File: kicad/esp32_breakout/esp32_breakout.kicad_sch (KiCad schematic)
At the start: 21 parts, among them J1 JST PH 2mm 7-pin male thru ve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, J2 JST PH 5-pin male thru vertic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, J3 JST PH 6-pin male thru vertic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, J4 Barrel_Jack, J5 JST PH 5-pin male thru vertic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, J6 JST PH 6-pin male thru vertic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, J7 JST PH 6-pin male thru vertic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, Q1 BSS123, SW1 SS12D10, U1 ESP32 DEV KIT DOIT 30-pin, U2 MH-KC24

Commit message: KiCad PCB schematic
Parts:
- added J10, J14: Conn_02x04_Top_Bottom, Connector_PinHeader_2.54mm:PinHeader_2x04_P2.54mm_Vertical, symbol Connector_Generic:Conn_02x04_Top_Bottom
- added J11, J12, J13: JST PH 6-pin male thru vertical, Connector_JST:JST_PH_B6B-PH-K_1x06_P2.00mm_Vertical, symbol Connector_Generic:Conn_01x06
- added J8: Conn_01x05, Connector_PinHeader_2.54mm:PinHeader_1x05_P2.54mm_Vertical, symbol Connector_Generic:Conn_01x05
- added J9: Conn_01x03, Connector_PinHeader_2.54mm:PinHeader_1x03_P2.54mm_Vertical, symbol Connector_Generic:Conn_01x03
- added R10: 10k, Resistor_SMD:R_0603_1608Metric, symbol Device:R_Small_US
- D1: value 1N4004 -> CGRA4004-G; footprint (none) -> Diode_SMD:D_SMA
- J4: value Barrel_Jack -> DC-005 5.5x2.1mm; footprint (none) -> Connector_BarrelJack:BarrelJack_GCT_DCJ200-10-A_Horizontal
- SW1: footprint (none) -> Library:SIP-3
- U1: footprint (none) -> Library:DIP-30_1000_ELL
- U2: value MH-KC24 -> Mini560-Pro; footprint (none) -> Library:SOIC-4; Link https://www.aliexpress.us/item/3256802247317350.html -> https://www.aliexpress.us/item/3256801443409123.html; Type USB Step Down Module 24V Dual Output -> DC-DC Module
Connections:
- net TOUCH6_TBD is gone; now on net I2C_INT: U1.26 (RTC_GPIO16/HSPI_CLK/TOUCH6/ADC2_CH6/GPIO14_BOOT_PWM)
- net +24V: now also U2.4 (VIN+); no longer U2.1 (VIN)
- net +3V3: now also J11.2 (Pin_2), J12.2 (Pin_2), J13.2 (Pin_2), J14.5 (Pin_5), J14.6 (Pin_6), J14.7 (Pin_7), J14.8 (Pin_8)
- net +5V: now also U2.3 (VOUT+), J11.1 (Pin_1), J12.1 (Pin_1), J13.1 (Pin_1), J14.1 (Pin_1), J14.2 (Pin_2), J14.3 (Pin_3), J14.4 (Pin_4), J8.1 (Pin_1), J9.1 (Pin_1); no longer U2.2 (VOUT)
- net GND: now also U2.1 (VIN-), U2.2 (VOUT-), J10.5 (Pin_5), J10.6 (Pin_6), J10.7 (Pin_7), J10.8 (Pin_8), J11.6 (Pin_6), J12.6 (Pin_6), J13.6 (Pin_6), J8.4 (Pin_4), J8.5 (Pin_5), J9.3 (Pin_3); no longer J5.3 (Pin_3), U1.23 (RTC_GPIO6/DAC1/ADC2_CH8/GPIO25), U2.3 (GND)
- net I2C_INT: now also J11.5 (Pin_5), J12.5 (Pin_5), J13.5 (Pin_5); no longer U1.18 (RTC_GPIO3/SENSOR_VN/ADC1_CH3/GPIO39_IN)
- net I2C_SCL: now also J11.3 (Pin_3), J12.3 (Pin_3), J13.3 (Pin_3)
- net I2C_SDA: now also J11.4 (Pin_4), J12.4 (Pin_4), J13.4 (Pin_4)
- net GPIO5_BOOT_STRAP: now reaches U1.8 (BOOT_PWM_GPIO5/VSPI_CS0)
- net GPIO5_BOOT_STRAP: now also J9.2 (Pin_2)
- net SERVO_LEFT renamed GPIO26_TOUCH
- net GPIO26_TOUCH: now also J10.3 (Pin_3)
- net SERVO_RIGHT renamed GPIO27_TOUCH
- net GPIO27_TOUCH: now also J10.2 (Pin_2)
- net TOUCH0 renamed GPIO4_TOUCH
- net GPIO4_TOUCH: now also J10.4 (Pin_4)
- net TOUCH5_TBD renamed GPIO12_OUT_STRAP
- net GPIO12_OUT_STRAP: now also J8.2 (Pin_2)
- net TOUCH9 renamed GPIO32_TOUCH
- net GPIO32_TOUCH: now also J10.1 (Pin_1)
- new net: J8.3 (Pin_3), R10.2
- new net GPIO39_IN: R10.1, U1.18 (RTC_GPIO3/SENSOR_VN/ADC1_CH3/GPIO39_IN)
- new net MOT_CW_RIGHT: J5.3 (Pin_3), U1.23 (RTC_GPIO6/DAC1/ADC2_CH8/GPIO25)
- no-connect marks 5 -> 4
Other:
- note added: "GPIO"
- note added: "I2C EXPANSION"
- note added: "LASER POINTER"
- note added: "SONAR"
- note removed: "BATTERY CONNECTOR"
- note removed: "EXPANSION"
- note removed: "TODO - on/off switch footprint - sonar conn? radar conn? - Try GPIO14_BOOT_PWM TOUCH6 - Try GPIO12_OUT TOUCH5 - regulator module connections - charger? - ESP32 footprint - TOUCH connector?"
- moved on the sheet: J3, J4, J6, J7, R5, R6, R9, SW1, U1

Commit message: Schematic WIP
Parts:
- removed J14: Conn_02x04_Top_Bottom, Connector_PinHeader_2.54mm:PinHeader_2x04_P2.54mm_Vertical, symbol Connector_Generic:Conn_02x04_Top_Bottom
- removed J4: DC-005 5.5x2.1mm, Connector_BarrelJack:BarrelJack_GCT_DCJ200-10-A_Horizontal, symbol Connector:Barrel_Jack
- removed SW1: SS12D10, Library:SIP-3, symbol Switch:SW_SPST
- added J4: DC-005 5.5x2.1mm, Connector_BarrelJack:BarrelJack_GCT_DCJ200-10-A_Horizontal, symbol Connector:Barrel_Jack_Switch
- added J5: Deans T-Plug M, Makerspet:DEANS-T-PLUG, symbol Makerspet:Deans T-Plug
- added SW1: SS12D10, Makerspet:SWITCH, symbol Switch:SW_SPDT
- J1: renamed from J5; value JST PH 5-pin male thru vertical -> JST PH F
- J10: renamed from J6; value JST PH 6-pin male thru vertical -> JST PH F
- J11: renamed from J7; value JST PH 6-pin male thru vertical -> JST PH F
- J12: renamed from J11; value JST PH 6-pin male thru vertical -> JST PH F
- J13: renamed from J12; value JST PH 6-pin male thru vertical -> JST PH F
- J14: renamed from J13; value JST PH 6-pin male thru vertical -> JST PH F
- J2: value JST PH 5-pin male thru vertical -> JST PH F
- J3: renamed from J1; value JST PH 2mm 7-pin male thru vertical -> JST PH F; footprint (none) -> Connector_JST:JST_PH_B7B-PH-K_1x07_P2.00mm_Vertical
- J6: renamed from J10; value Conn_02x04_Top_Bottom -> Header F
- J7: renamed from J8; value Conn_01x05 -> Header F
- J8: renamed from J9; value Conn_01x03 -> Header F
- J9: renamed from J3; value JST PH 6-pin male thru vertical -> JST PH F
- U1: value ESP32 DEV KIT DOIT 30-pin -> ESP32 DEV KIT 30-pin; footprint Library:DIP-30_1000_ELL -> Makerspet:ESP-32; symbol Kaia_v2:ESP32-DOIT-V1 -> Makerspet:ESP32-DOIT-V1
- U2: footprint Library:SOIC-4 -> Makerspet:Mini560-Pro; symbol Snoopy:USB-Step-Down-Converter -> Makerspet:DC-DC
- renumbered R2 to R1, R9 to R10, R4 to R2, R1 to R4, R8 to R5, R7 to R6, R10 to R7, R5 to R8, R6 to R9
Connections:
- net +24V: now also SW1.2 (B)
- net +3V3: now also J6.6 (Pin_6)
- net +5V: now also J6.5 (Pin_5)
- net GND: now also J4.2, J5.2 (BAT-); no longer J6.5 (Pin_5), J6.6 (Pin_6)
- new net +BATT: J4.1, J5.1 (BAT+), SW1.1 (A)
- no-connect marks 4 -> 6
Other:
- note added: "- add T plug - DC-005 as charger plug - BEFORE switch - IN CASE battery charges from input - barrel jack location?"
- company: REMAKE.AI -> Maker's Pet
- title: ESP32 Breakout -> Maker's Pet ESP32 Breakout
- moved on the sheet: J10, J11, J12, J13, J14, J6, J7, J8, R7

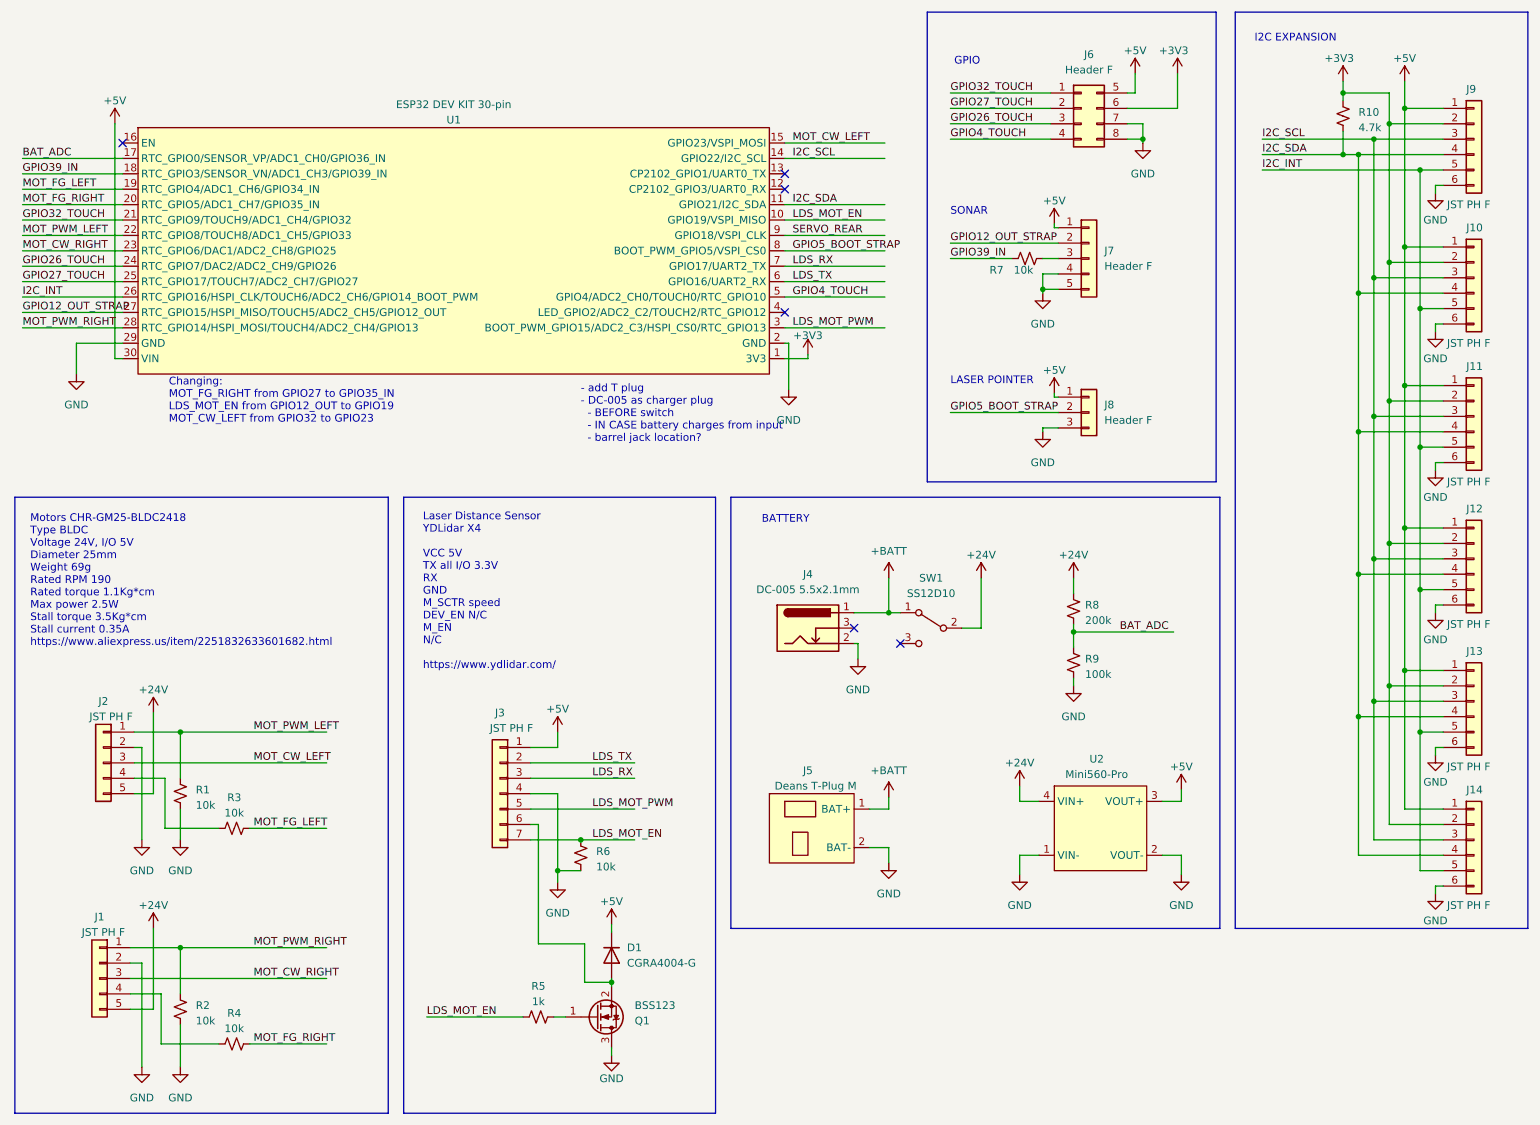
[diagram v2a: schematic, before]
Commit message: Fix broken fw; ESP32 schematic
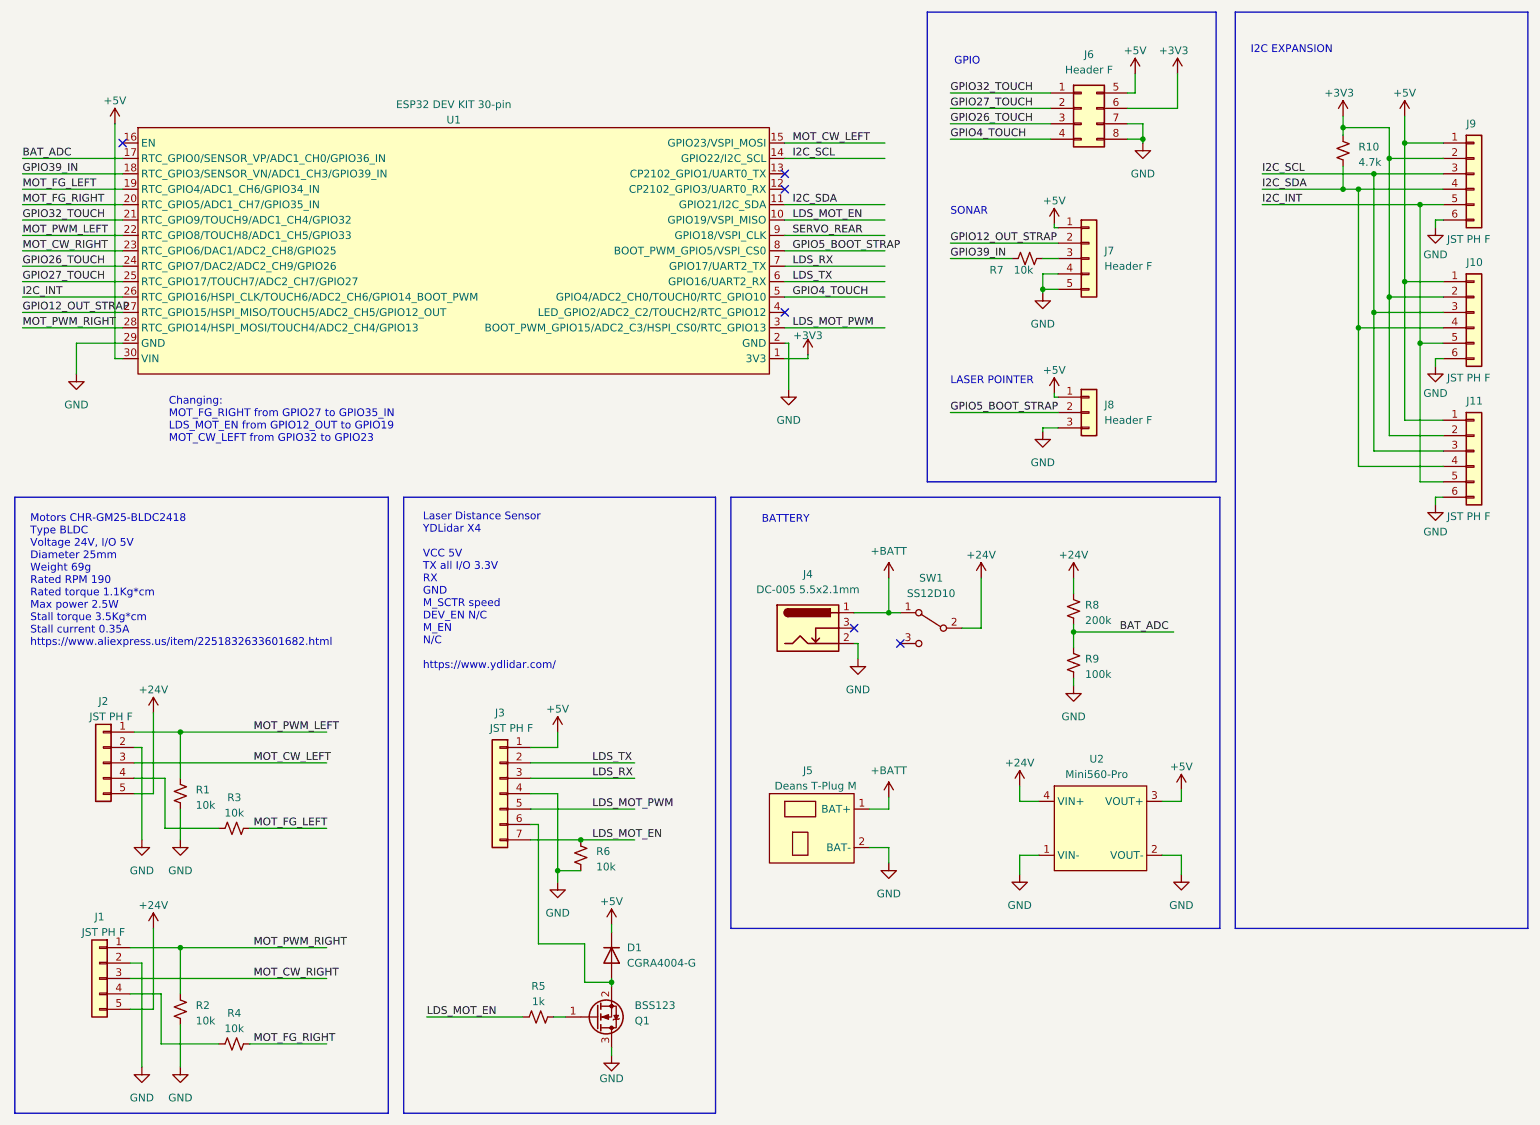
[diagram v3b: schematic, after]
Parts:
- removed J12, J13, J14: JST PH F, Connector_JST:JST_PH_B6B-PH-K_1x06_P2.00mm_Vertical, symbol Connector_Generic:Conn_01x06
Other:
- note removed: "- add T plug - DC-005 as charger plug - BEFORE switch - IN CASE battery charges from input - barrel jack location?"
- moved on the sheet: J10, J11, J9, R10

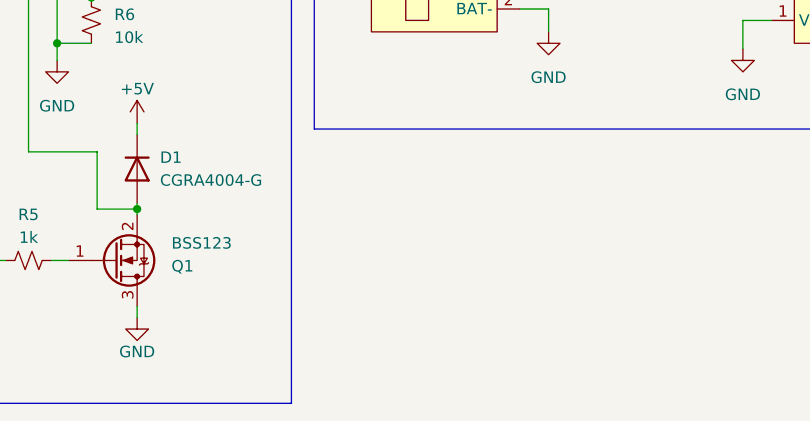
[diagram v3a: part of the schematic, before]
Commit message: Layout DRC pass
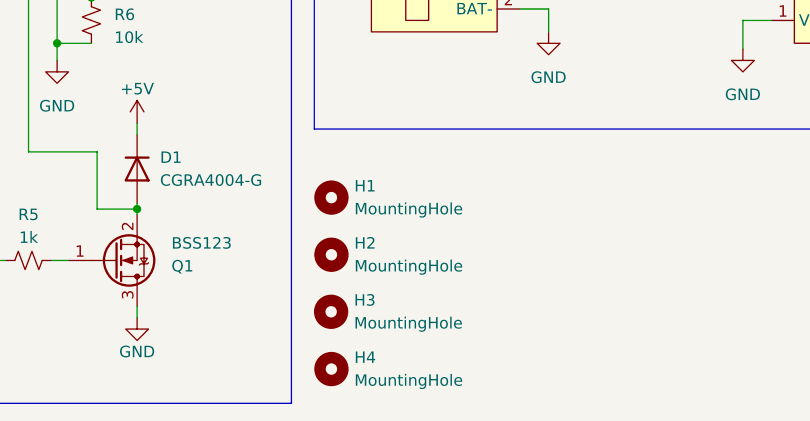
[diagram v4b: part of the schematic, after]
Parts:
- added H1, H2, H3, H4: MountingHole, MountingHole:MountingHole_3.2mm_M3, symbol Mechanical:MountingHole
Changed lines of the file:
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@@
+    )
+  )
+  (symbol (lib_id "Mechanical:MountingHole") (at 134.62 173.99 0) (unit 1)
+    (in_bom yes) (on_board yes) (dnp no) (fields_autoplaced)
+    (property "Reference" "H1" (at 137.16 172.72 0)
+      (effects (font (size 1.27 1.27)) (justify left))
+    )
+    (property "Value" "MountingHole" (at 137.16 175.26 0)
+      (effects (font (size 1.27 1.27)) (justify left))
+    )
+    (property "Footprint" "MountingHole:MountingHole_3.2mm_M3" (at 134.62 173.99 0)
+      (effects (font (size 1.27 1.27)) hide)
+    )
+    (property "Datasheet" "~" (at 134.62 173.99 0)
+      (effects (font (size 1.27 1.27)) hide)
+    )
+    (instances
+      (project "esp32_breakout"
+        (path "/e24ae185-8f18-408c-aee8-f727519bade3"
+          (reference "H1") (unit 1)
+        )
+      )
     )
   )
@@
         (path "/e24ae185-8f18-408c-aee8-f727519bade3"
           (reference "#PWR029") (unit 1)
+        )
+      )
+    )
+  )
+  (symbol (lib_id "Mechanical:MountingHole") (at 134.62 193.04 0) (unit 1)
+    (in_bom yes) (on_board yes) (dnp no) (fields_autoplaced)
+    (property "Reference" "H4" (at 137.16 191.77 0)
+      (effects (font (size 1.27 1.27)) (justify left))
+    )
+    (property "Value" "MountingHole" (at 137.16 194.31 0)
+      (effects (font (size 1.27 1.27)) (justify left))
+    )
+    (property "Footprint" "MountingHole:MountingHole_3.2mm_M3" (at 134.62 193.04 0)
+      (effects (font (size 1.27 1.27)) hide)
+    )
+    (property "Datasheet" "~" (at 134.62 193.04 0)
+      (effects (font (size 1.27 1.27)) hide)
+    )
+    (instances
+      (project "esp32_breakout"
+        (path "/e24ae185-8f18-408c-aee8-f727519bade3"
+          (reference "H4") (unit 1)
         )
       )
@@
     )
   )
+  (symbol (lib_id "Mechanical:MountingHole") (at 134.5851 186.6785 0) (unit 1)
+    (in_bom yes) (on_board yes) (dnp no) (fields_autoplaced)
+    (property "Reference" "H3" (at 137.1251 185.4085 0)
+      (effects (font (size 1.27 1.27)) (justify left))
+    )
+    (property "Value" "MountingHole" (at 137.1251 187.9485 0)
+      (effects (font (size 1.27 1.27)) (justify left))
+    )
+    (property "Footprint" "MountingHole:MountingHole_3.2mm_M3" (at 134.5851 186.6785 0)
+      (effects (font (size 1.27 1.27)) hide)
+    )
+    (property "Datasheet" "~" (at 134.5851 186.6785 0)
+      (effects (font (size 1.27 1.27)) hide)
+    )
+    (instances
+      (project "esp32_breakout"
+        (path "/e24ae185-8f18-408c-aee8-f727519bade3"
+          (reference "H3") (unit 1)
+        )
+      )
+    )
+  )
   (symbol (lib_id "power:+5V") (at 104.14 133.985 0) (unit 1)
     (in_bom yes) (on_board yes) (dnp no) (fields_autoplaced)
@@
         )
       )
+    )
+  )
+  (symbol (lib_id "Mechanical:MountingHole") (at 134.62 180.34 0) (unit 1)
+    (in_bom yes) (on_board yes) (dnp no) (fields_autoplaced)
+    (property "Reference" "H2" (at 137.16 179.07 0)
+      (effects (font (size 1.27 1.27)) (justify left))
+    )
+    (property "Value" "MountingHole" (at 137.16 181.61 0)
+      (effects (font (size 1.27 1.27)) (justify left))
+    )
+    (property "Footprint" "MountingHole:MountingHole_3.2mm_M3" (at 134.62 180.34 0)
+      (effects (font (size 1.27 1.27)) hide)
+    )
+    (property "Datasheet" "~" (at 134.62 180.34 0)
+      (effects (font (size 1.27 1.27)) hide)
+    )
+    (instances
+      (project "esp32_breakout"
+        (path "/e24ae185-8f18-408c-aee8-f727519bade3"
+          (reference "H2") (unit 1)
+        )
+      )

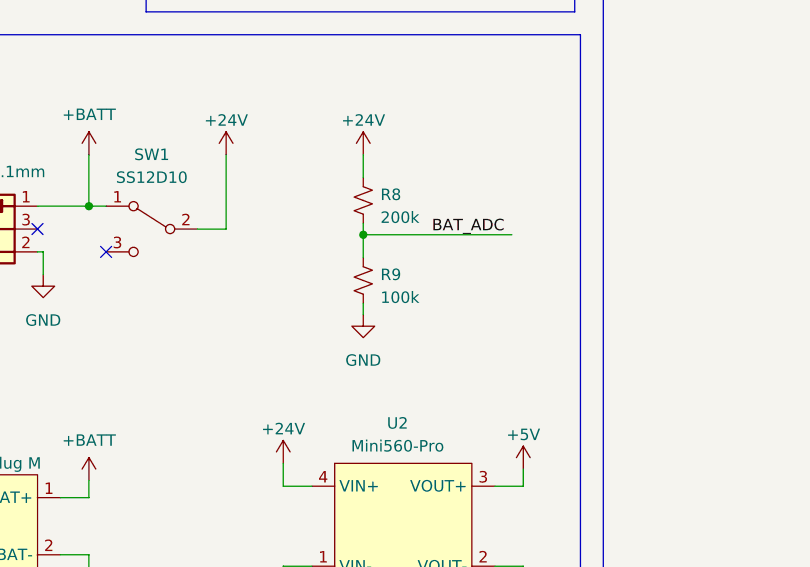
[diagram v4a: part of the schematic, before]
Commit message: Schematic, BOM R9 fix
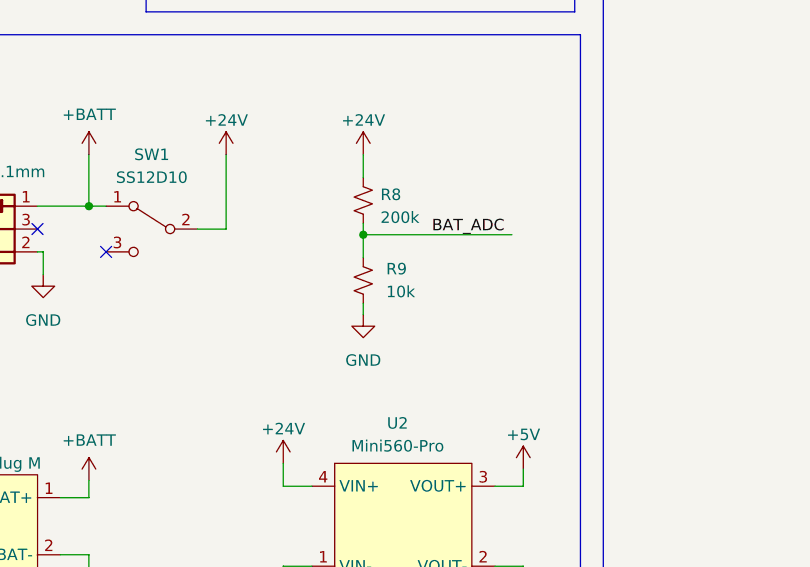
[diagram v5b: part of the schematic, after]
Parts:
- R9: value 100k -> 10k
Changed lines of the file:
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@@
   (symbol (lib_id "Device:R_Small_US") (at 189.23 122.555 180) (unit 1)
     (in_bom yes) (on_board yes) (dnp no) (fields_autoplaced)
-    (property "Reference" "R9" (at 191.135 121.92 0)
+    (property "Reference" "R9" (at 191.77 121.285 0)
       (effects (font (size 1.27 1.27)) (justify right))
     )
-    (property "Value" "100k" (at 191.135 124.46 0)
+    (property "Value" "10k" (at 191.77 123.825 0)
       (effects (font (size 1.27 1.27)) (justify right))
     )
